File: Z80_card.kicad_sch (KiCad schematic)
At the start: 16 parts, among them J1 Conn_02x20_Counter_Clockwise_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, J2 Conn_01x03_Pin, J3 Conn_01x01_Pin, U1 Z84C00-4SC

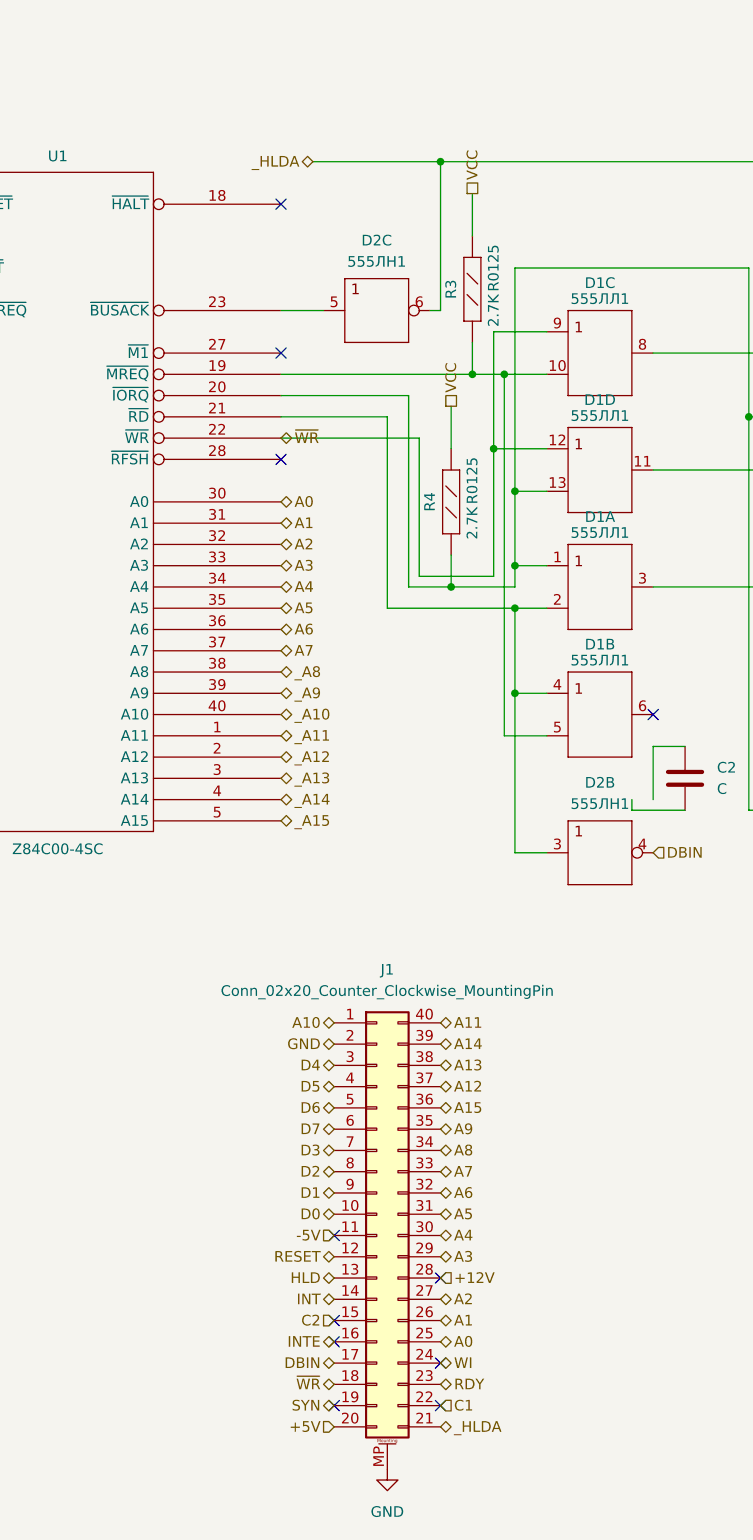
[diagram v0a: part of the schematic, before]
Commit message: Fix address and data buffering
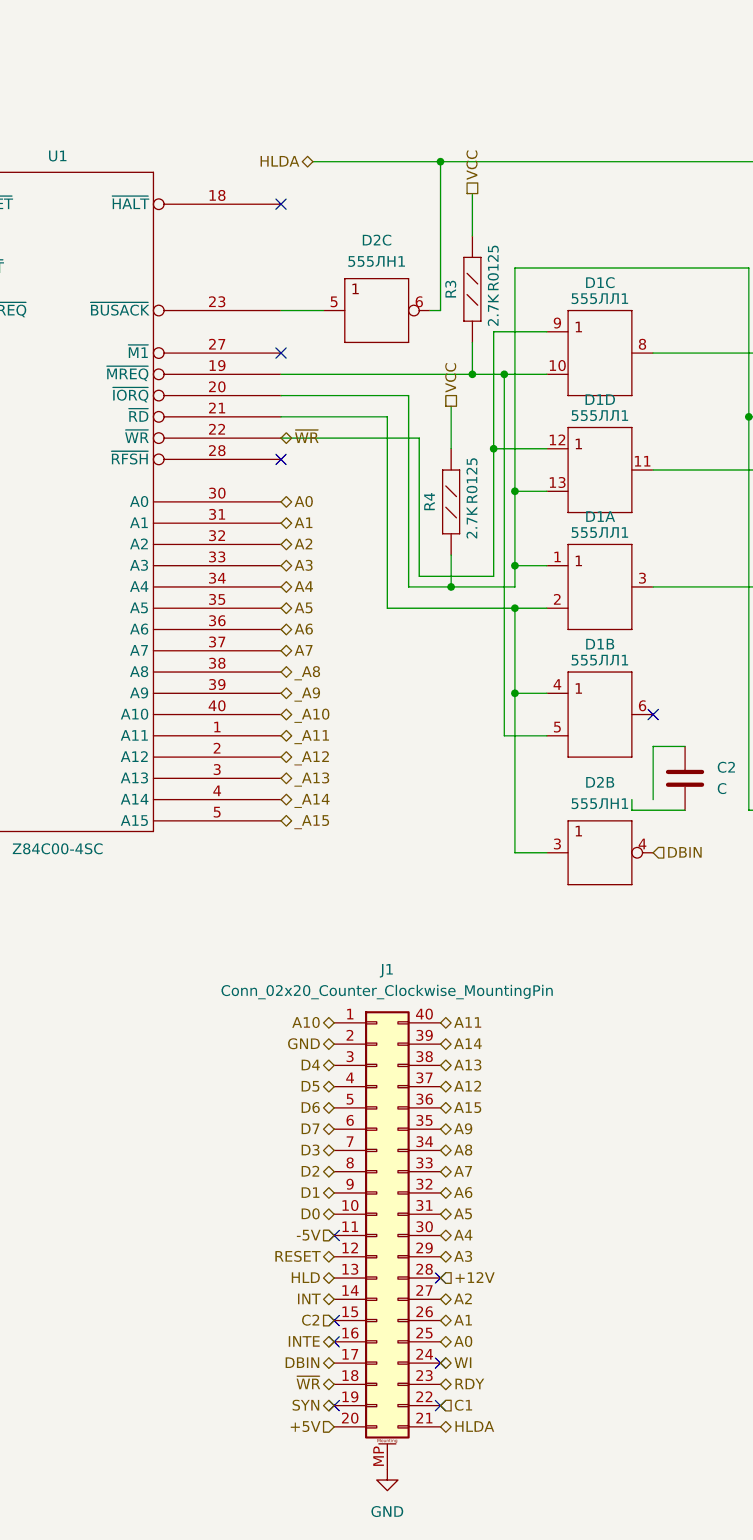
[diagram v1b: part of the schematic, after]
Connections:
- net _HLDA renamed HLDA
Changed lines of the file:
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@@
 		)
 	)
-	(hierarchical_label "_HLDA"
+	(hierarchical_label "HLDA"
 		(shape bidirectional)
 		(at 114.3 26.67 180)
@@
 		)
 	)
-	(hierarchical_label "_HLDA"
+	(hierarchical_label "HLDA"
 		(shape bidirectional)
 		(at 129.54 177.8 0)
